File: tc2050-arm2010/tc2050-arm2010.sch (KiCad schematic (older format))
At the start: 6 parts, among them J1 Conn_02x05_Odd_Even, J2 Conn_02x10_Odd_Even

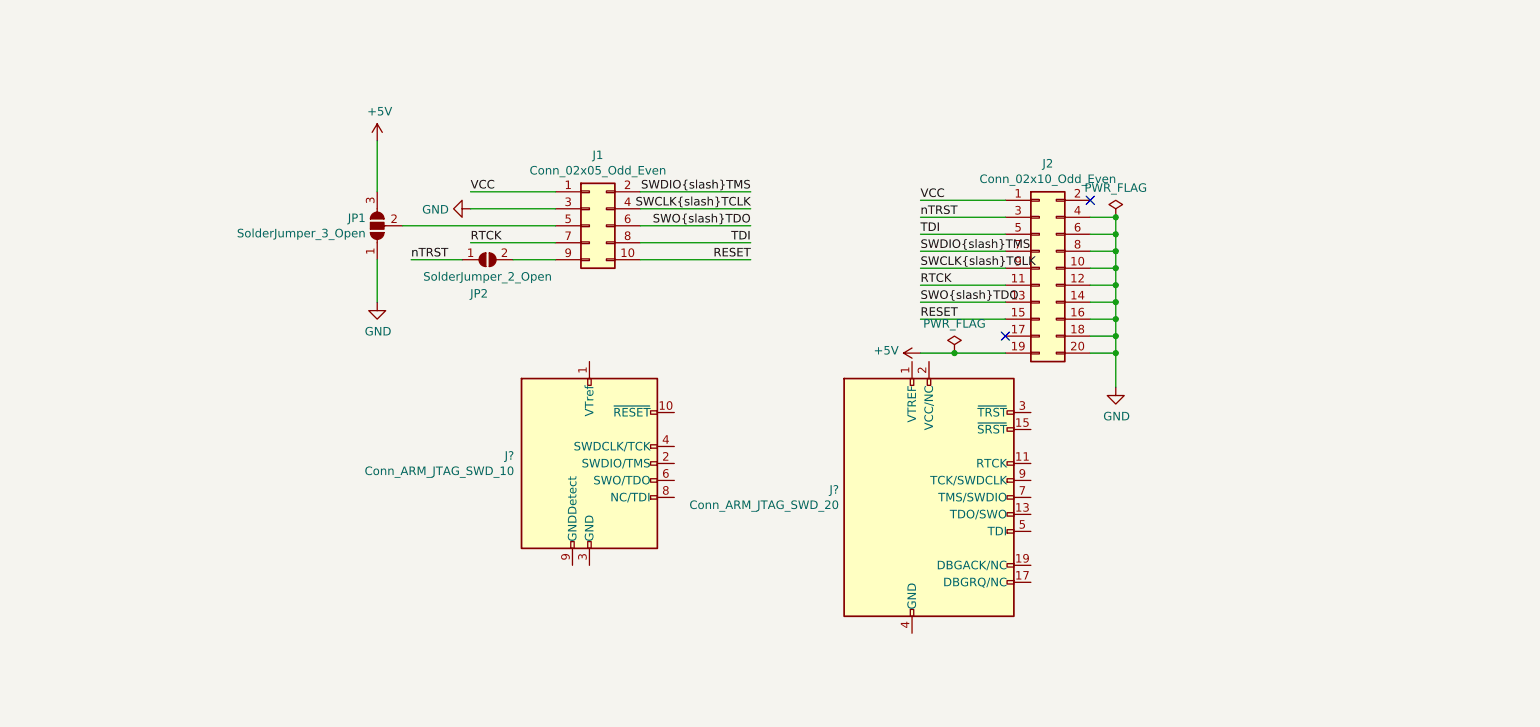
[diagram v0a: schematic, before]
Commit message: New version also has TC2030 header as well as ARM10 and breakaway board from ARM10 to 7-pin SWD
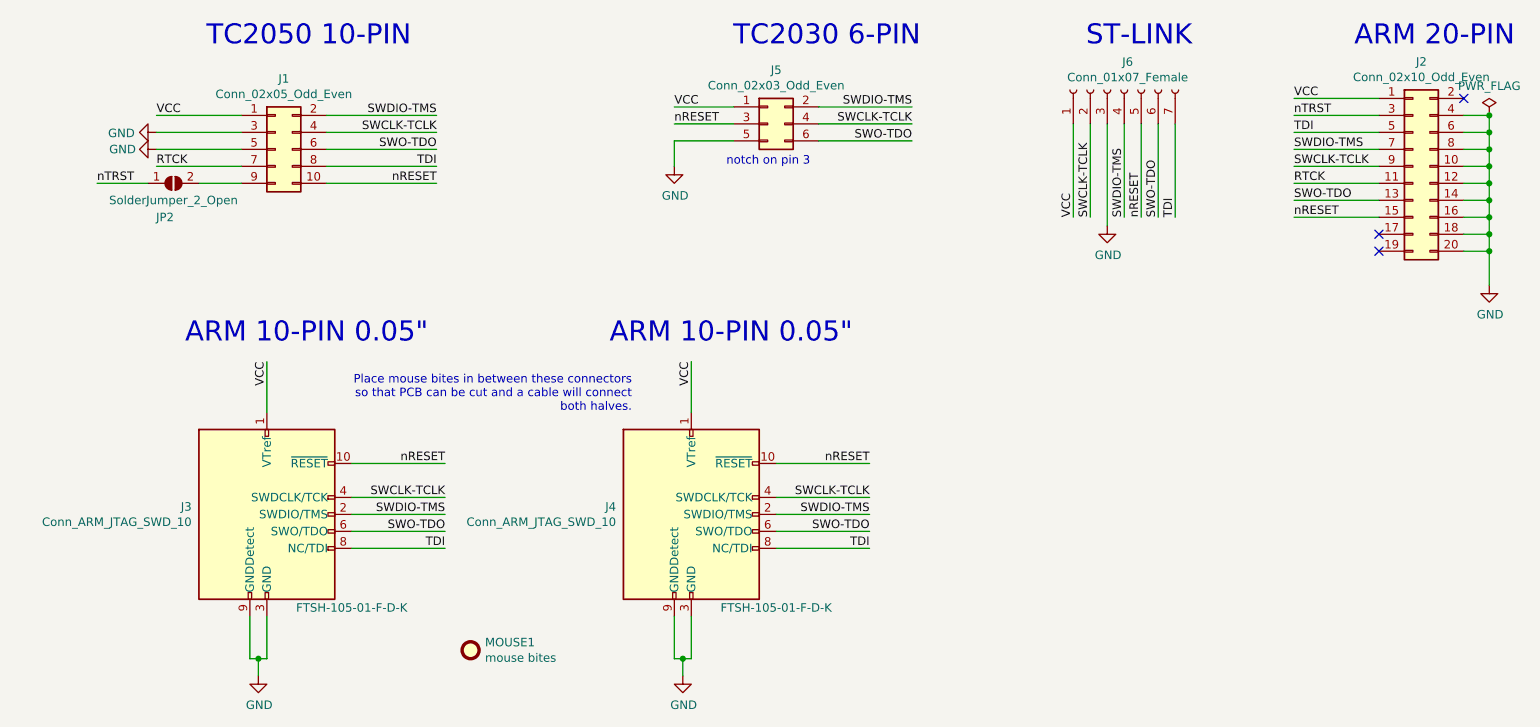
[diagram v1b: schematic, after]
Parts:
- removed J?: Conn_ARM_JTAG_SWD_20, symbol Connector:Conn_ARM_JTAG_SWD_20
- removed JP1: SolderJumper_3_Open, Jumper:SolderJumper-3_P1.3mm_Open_RoundedPad1.0x1.5mm, symbol Jumper:SolderJumper_3_Open
- added J4: Conn_ARM_JTAG_SWD_10, Connector_PCBEdge:Samtec_MECF-05-02-L-DV-WT_2x05_P1.27mm_Polarized_Socket_Horizontal, symbol Connector:Conn_ARM_JTAG_SWD_10
- added J5: Conn_02x03_Odd_Even, symbol Connector_Generic:Conn_02x03_Odd_Even
- added J6: Conn_01x07_Female, Connector_PinHeader_2.54mm:PinHeader_1x07_P2.54mm_Vertical, symbol Connector:Conn_01x07_Female
- added MOUSE1: mouse bites, tc2050-arm2010:mouse-bite-1mm-slot, symbol Mechanical:Fiducial
- J3: renamed from J?; footprint (none) -> Connector_PCBEdge:Samtec_MECF-05-02-L-DV-WT_2x05_P1.27mm_Polarized_Socket_Horizontal; Digikey (none) -> SAM8909-ND; Partno (none) -> FTSH-105-01-F-D-K
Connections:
- net RESET is gone; now on net nRESET: J1.10 (Pin_10), J2.15 (Pin_15)
- net SWCLK/TCLK is gone; now on net SWCLK-TCLK: J1.4 (Pin_4), J2.9 (Pin_9)
- net SWDIO/TMS is gone; now on net SWDIO-TMS: J1.2 (Pin_2), J2.7 (Pin_7)
- net SWO/TDO is gone; now on net SWO-TDO: J1.6 (Pin_6), J2.13 (Pin_13)
- net GND: now also J1.5 (Pin_5), J3.3 (GND), J3.5 (GND), J3.9 (GNDDetect), J4.3 (GND), J4.5 (GND), J4.9 (GNDDetect), J5.5 (Pin_5), J6.3 (Pin_3)
- net TDI: now also J3.8 (NC/TDI), J4.8 (NC/TDI), J6.7 (Pin_7)
- net VCC: now also J3.1 (VTref), J4.1 (VTref), J5.1 (Pin_1), J6.1 (Pin_1)
- net nRESET: now reaches J3.10 (~RESET~)
- net nRESET: now also J4.10 (~RESET~), J5.3 (Pin_3), J6.5 (Pin_5)
- net SWDIO-TMS: now reaches J3.2 (SWDIO/TMS)
- net SWDIO-TMS: now also J4.2 (SWDIO/TMS), J5.2 (Pin_2), J6.4 (Pin_4)
- net SWCLK-TCLK: now reaches J3.4 (SWDCLK/TCK)
- net SWCLK-TCLK: now also J4.4 (SWDCLK/TCK), J5.4 (Pin_4), J6.2 (Pin_2)
- net SWO-TDO: now reaches J3.6 (SWO/TDO)
- net SWO-TDO: now also J4.6 (SWO/TDO), J5.6 (Pin_6), J6.6 (Pin_6)
- net +5V: no longer names the net of J2.19 (Pin_19)
- no-connect marks 2 -> 3
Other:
- note added: "ARM 10-PIN 0.05""
- note added: "ARM 20-PIN"
- note added: "Place mouse bites in between these connectors\nso that PCB can be cut and a cable will connect\nboth halves."
- note added: "ST-LINK"
- note added: "TC2030 6-PIN"
- note added: "TC2050 10-PIN"
- note added: "notch on pin 3"
- moved on the sheet: J1, J2, J3, JP2
